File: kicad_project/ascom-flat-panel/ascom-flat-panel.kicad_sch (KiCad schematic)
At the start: 12 parts, among them J1 Servo, J3 JST-XH LED, Q1 FQP30N06L, Q2 FQP30N06L, U1 SeeeduinoXIAO

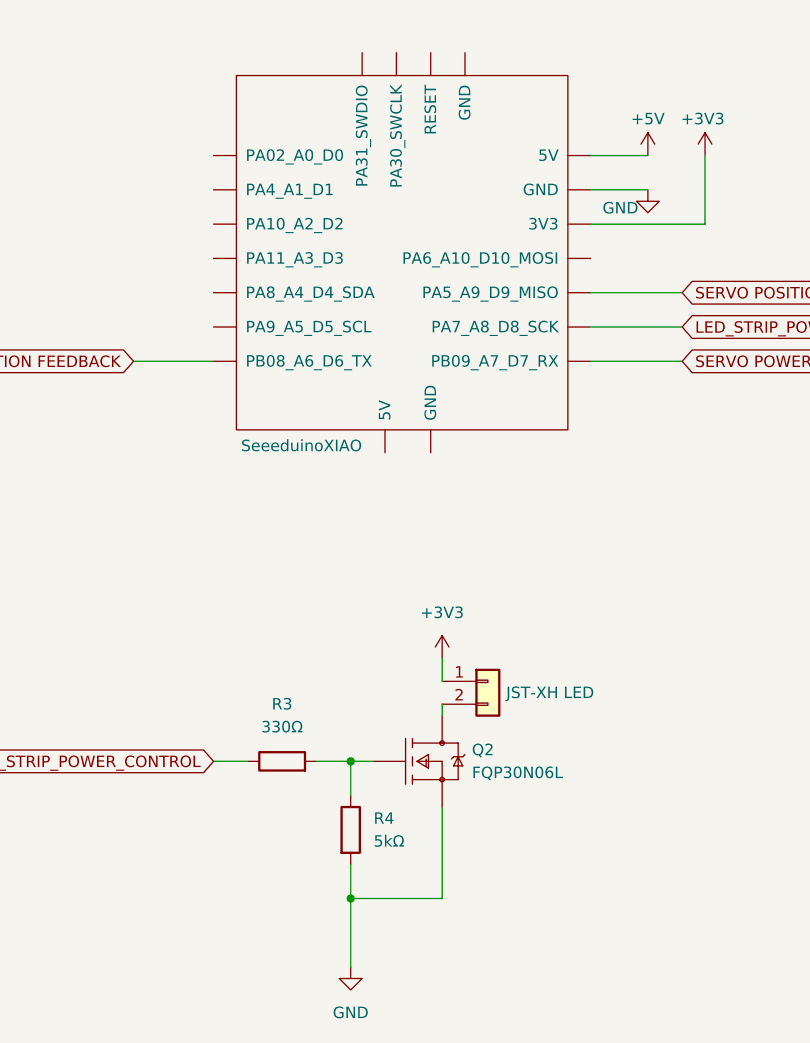
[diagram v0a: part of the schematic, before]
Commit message: ajout des bibliothèque de symboles et empreintes Seeeduino XIAO + mise à jour du schéma avec ces éléments + draft de pcb
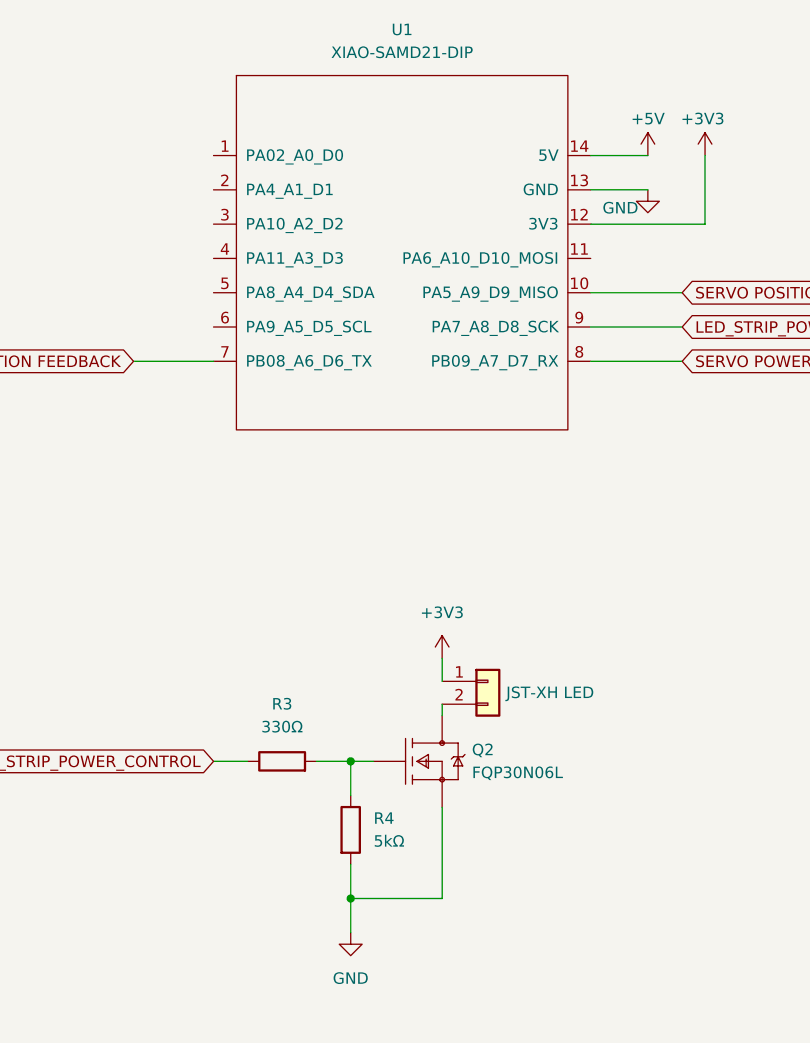
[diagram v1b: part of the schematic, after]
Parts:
- removed U1: SeeeduinoXIAO, Seeeduino XIAO:Seeeduino XIAO-MOUDLE14P-2.54-21X17.8MM, symbol Seeeduino XIAO:SeeeduinoXIAO
- added U1: XIAO-SAMD21-DIP, Seeeduino XIAO:XIAO-SAMD21-DIP, symbol Seeeduino:XIAO-SAMD21-DIP
- Q1, Q2: footprint MyFootprints:FQP30N06L -> Package_TO_SOT_THT:TO-220-3_Vertical
- R3, R4: footprint (none) -> Resistor_THT:R_Axial_DIN0207_L6.3mm_D2.5mm_P10.16mm_Horizontal
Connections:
- net +3V3: now also U1.12 (3V3)
- net +5V: now also U1.14 (5V)
- net GND: now also U1.13 (GND)
- net LED_STRIP_POWER_CONTROL: now also U1.9 (PA7_A8_D8_SCK)
- net SERVO POSITION CONTROL: now also U1.10 (PA5_A9_D9_MISO)
- net SERVO POSITION FEEDBACK: now also U1.7 (PB08_A6_D6_TX)
- net SERVO POWER CONTROL: now also U1.8 (PB09_A7_D7_RX)
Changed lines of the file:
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@@
 	(wire
 		(pts
-			(xy 78.74 127) (xy 78.74 134.62)
+			(xy 78.74 127) (xy 78.74 130.81)
 		)
 		(stroke
@@
 			)
 		)
-		(property "Footprint" ""
+		(property "Footprint" "Resistor_THT:R_Axial_DIN0207_L6.3mm_D2.5mm_P10.16mm_Horizontal"
 			(at 76.962 119.38 90)
 			(effects
@@
 	)
 	(symbol
-		(lib_id "Seeeduino XIAO:SeeeduinoXIAO")
-		(at 85.09 55.88 0)
-		(unit 1)
-		(exclude_from_sim no)
-		(in_bom yes)
-		(on_board yes)
-		(dnp no)
-		(property "Reference" "U1"
-			(at 89.8241 77.47 0)
-			(effects
-				(font
-					(size 1.27 1.27)
-				)
-				(justify left)
-				(hide yes)
-			)
-		)
-		(property "Value" "SeeeduinoXIAO"
-			(at 66.548 76.708 0)
-			(effects
-				(font
-					(size 1.27 1.27)
-				)
-				(justify left)
-			)
-		)
-		(property "Footprint" "Seeeduino XIAO:Seeeduino XIAO-MOUDLE14P-2.54-21X17.8MM"
-			(at 76.2 50.8 0)
-			(effects
-				(font
-					(size 1.27 1.27)
-				)
-				(hide yes)
-			)
-		)
-		(property "Datasheet" ""
-			(at 76.2 50.8 0)
-			(effects
-				(font
-					(size 1.27 1.27)
-				)
-				(hide yes)
-			)
-		)
-		(property "Description" ""
-			(at 85.09 55.88 0)
-			(effects
-				(font
-					(size 1.27 1.27)
-				)
-			)
-		)
-		(pin "12"
-		)
-		(pin "10"
-		)
-		(pin "16"
-		)
-		(pin "15"
-		)
-		(pin "2"
-		)
-		(pin "17"
-		)
-		(pin "3"
-		)
-		(pin "4"
-		)
-		(pin "5"
-		)
-		(pin "19"
-		)
-		(pin "18"
-		)
-		(pin "20"
-		)
-		(pin "8"
-		)
-		(pin "9"
-		)
-		(pin "6"
-		)
-		(pin "7"
-		)
-		(pin "14"
-		)
-		(pin "13"
-		)
-		(pin "11"
-		)
-		(pin "1"
-		)
-		(instances
-			(project "TelescopeCoverV2-Simple"
-				(path "/c93103f3-9ac9-4319-baa6-df31525a6c92"
-					(reference "U1")
-					(unit 1)
-				)
-			)
-		)
-	)
-	(symbol
 		(lib_id "DarkSkyGeek_KiCad_Symbol_Library:FQP30N06L")
 		(at 182.88 111.76 0)
@@
 			)
 		)
-		(property "Footprint" "MyFootprints:FQP30N06L"
+		(property "Footprint" "Package_TO_SOT_THT:TO-220-3_Vertical"
 			(at 182.88 99.06 0)
 			(effects
@@
 			)
 		)
-		(property "Footprint" ""
+		(property "Footprint" "Resistor_THT:R_Axial_DIN0207_L6.3mm_D2.5mm_P10.16mm_Horizontal"
 			(at 71.12 113.538 90)
 			(effects
@@
 				(path "/c93103f3-9ac9-4319-baa6-df31525a6c92"
 					(reference "#PWR02")
+					(unit 1)
+				)
+			)
+		)
+	)
+	(symbol
+		(lib_id "Seeeduino:XIAO-SAMD21-DIP")
+		(at 85.09 55.88 0)
+		(unit 1)
+		(exclude_from_sim no)
+		(in_bom yes)
+		(on_board yes)
+		(dnp no)
+		(fields_autoplaced yes)
+		(property "Reference" "U1"
+			(at 84.455 30.48 0)
+			(effects
+				(font
+					(size 1.27 1.27)
+				)
+			)
+		)
+		(property "Value" "XIAO-SAMD21-DIP"
+			(at 84.455 33.02 0)
+			(effects
+				(font
+					(size 1.27 1.27)
+				)
+			)
+		)
+		(property "Footprint" "Seeeduino XIAO:XIAO-SAMD21-DIP"
+			(at 76.2 50.8 0)
+			(effects
+				(font
+					(size 1.27 1.27)
+				)
+				(hide yes)
+			)
+		)
+		(property "Datasheet" ""
+			(at 76.2 50.8 0)
+			(effects
+				(font
+					(size 1.27 1.27)
+				)
+				(hide yes)
+			)
+		)
+		(property "Description" ""
+			(at 85.09 55.88 0)
+			(effects
+				(font
+					(size 1.27 1.27)
+				)
+				(hide yes)
+			)
+		)
+		(pin "3"
+		)
+		(pin "2"
+		)
+		(pin "5"
+		)
+		(pin "1"
+		)
+		(pin "14"
+		)
+		(pin "4"
+		)
+		(pin "6"
+		)
+		(pin "13"
+		)
+		(pin "12"
+		)
+		(pin "11"
+		)
+		(pin "10"
+		)
+		(pin "9"
+		)
+		(pin "8"
+		)
+		(pin "7"
+		)
+		(instances
+			(project ""
+				(path "/c93103f3-9ac9-4319-baa6-df31525a6c92"
+					(reference "U1")
 					(unit 1)
 				)
@@
 			)
 		)
-		(property "Footprint" "MyFootprints:FQP30N06L"
+		(property "Footprint" "Package_TO_SOT_THT:TO-220-3_Vertical"
 			(at 78.74 99.06 0)
 			(effects
@@
 		(lib_name "GND_1")
 		(lib_id "power:GND")
-		(at 78.74 134.62 0)
+		(at 78.74 130.81 0)
 		(unit 1)
 		(exclude_from_sim no)
@@
 		(fields_autoplaced yes)
 		(property "Reference" "#PWR09"
-			(at 78.74 140.97 0)
+			(at 78.74 137.16 0)
 			(effects
 				(font
@@
 		)
 		(property "Value" "GND"
-			(at 78.74 139.7 0)
+			(at 78.74 135.89 0)
 			(effects
 				(font
@@
 		)
 		(property "Footprint" ""
-			(at 78.74 134.62 0)
+			(at 78.74 130.81 0)
 			(effects
 				(font
@@
 		)
 		(property "Datasheet" ""
-			(at 78.74 134.62 0)
+			(at 78.74 130.81 0)
 			(effects
 				(font
@@
 		)
 		(property "Description" "Power symbol creates a global label with name \"GND\" , ground"
-			(at 78.74 134.62 0)
-			(effects
-				(font
+			(at 78.74 130.81 0)
+			(effects
+				(font

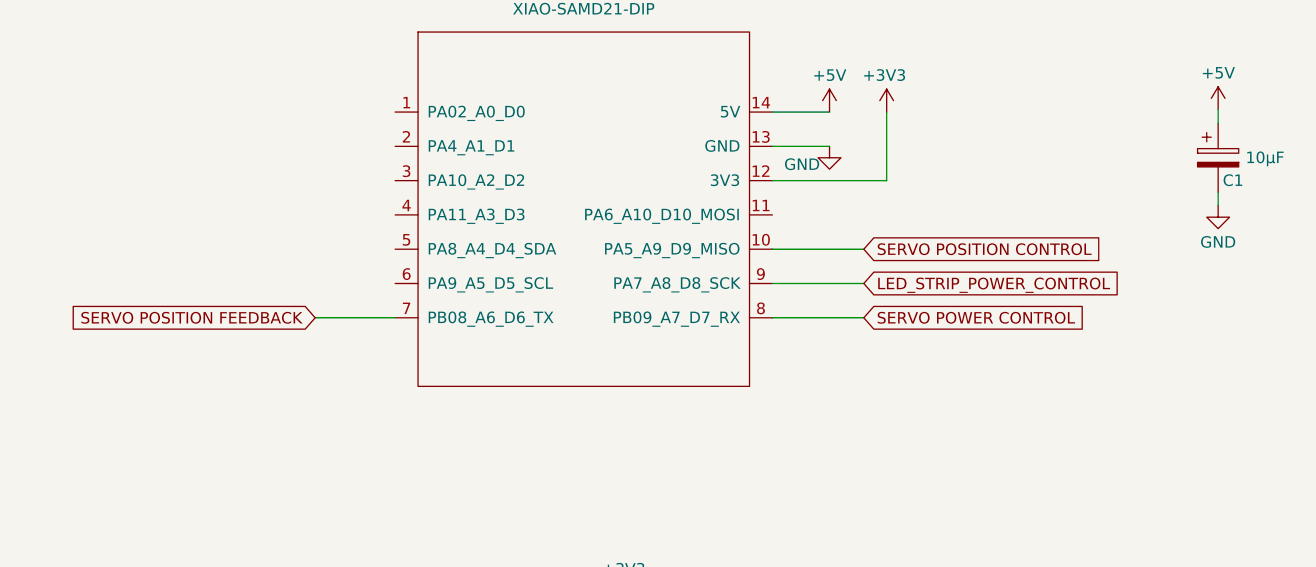
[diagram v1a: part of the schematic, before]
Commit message: Première mise en forme et routage du circuit - ajout modèle3D seeeduino
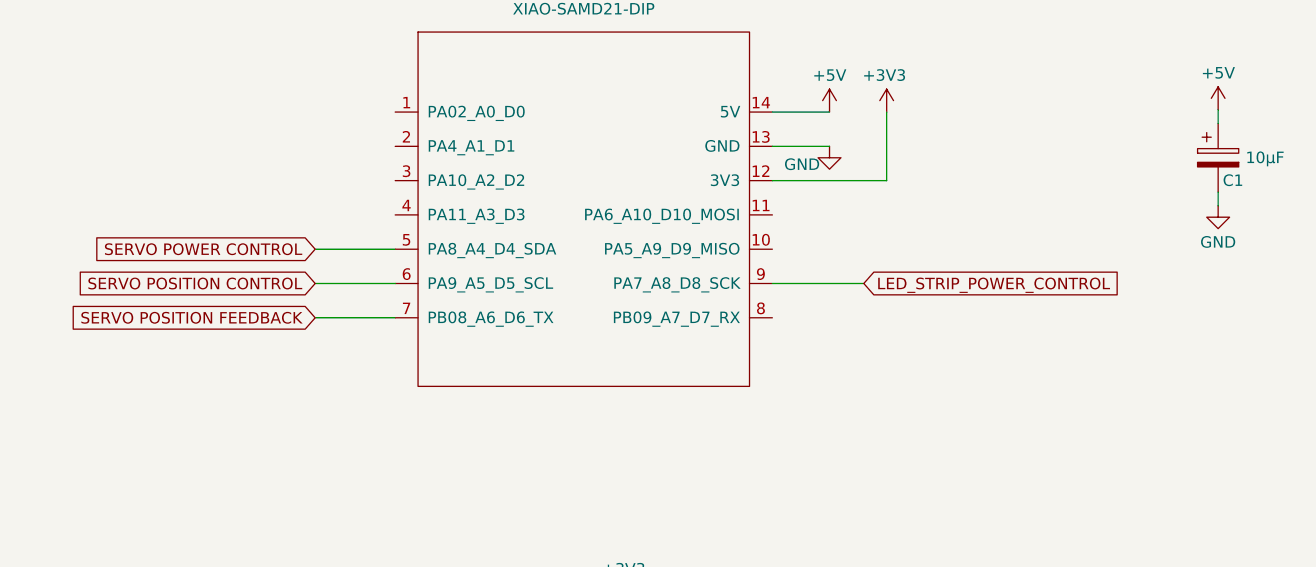
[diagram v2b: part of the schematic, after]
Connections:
- net SERVO POSITION CONTROL: now also U1.6 (PA9_A5_D5_SCL); no longer U1.10 (PA5_A9_D9_MISO)
- net SERVO POWER CONTROL: now also U1.5 (PA8_A4_D4_SDA); no longer U1.8 (PB09_A7_D7_RX)
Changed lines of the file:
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@@
-	(wire
-		(pts
-			(xy 105.41 67.31) (xy 115.57 67.31)
-		)
-		(stroke
-			(width 0)
-			(type default)
-		)
-	)
 	(wire
 		(pts
@@
 	(wire
 		(pts
+			(xy 54.61 59.69) (xy 63.5 59.69)
+		)
+		(stroke
+			(width 0)
+			(type default)
+		)
+	)
+	(wire
+		(pts
+			(xy 54.61 63.5) (xy 63.5 63.5)
+		)
+		(stroke
+			(width 0)
+			(type default)
+		)
+	)
+	(wire
+		(pts
 			(xy 182.88 111.76) (xy 185.42 111.76)
 		)
@@
 	(wire
 		(pts
-			(xy 105.41 59.69) (xy 115.57 59.69)
-		)
-		(stroke
-			(width 0)
-			(type default)
-		)
-	)
-	(wire
-		(pts
 			(xy 193.04 46.482) (xy 198.12 46.482)
 		)
@@
 	(global_label "SERVO POWER CONTROL"
 		(shape input)
-		(at 115.57 67.31 0)
-		(fields_autoplaced yes)
-		(effects
-			(font
-				(size 1.27 1.27)
-			)
-			(justify left)
-		)
-		(property "Intersheetrefs" "${INTERSHEET_REFS}"
-			(at 141.5361 67.31 0)
-			(effects
-				(font
-					(size 1.27 1.27)
-				)
-				(justify left)
+		(at 54.61 59.69 180)
+		(fields_autoplaced yes)
+		(effects
+			(font
+				(size 1.27 1.27)
+			)
+			(justify right)
+		)
+		(property "Intersheetrefs" "${INTERSHEET_REFS}"
+			(at 28.6439 59.69 0)
+			(effects
+				(font
+					(size 1.27 1.27)
+				)
+				(justify right)
 				(hide yes)
 			)
@@
 	(global_label "SERVO POSITION CONTROL"
 		(shape input)
-		(at 115.57 59.69 0)
-		(fields_autoplaced yes)
-		(effects
-			(font
-				(size 1.27 1.27)
-			)
-			(justify left)
-		)
-		(property "Intersheetrefs" "${INTERSHEET_REFS}"
-			(at 143.7134 59.69 0)
-			(effects
-				(font
-					(size 1.27 1.27)
-				)
-				(justify left)
-				(hide yes)
-			)
+		(at 54.61 63.5 180)
+		(fields_autoplaced yes)
+		(effects
+			(font
+				(size 1.27 1.27)
+			)
+			(justify right)
+		)
+		(property "Intersheetrefs" "${INTERSHEET_REFS}"
+			(at 26.4666 63.5 0)
+			(effects
+				(font
+					(size 1.27 1.27)
+				)
+				(justify right)
+				(hide yes)
+			)

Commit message: Remplissage cartouche du schéma
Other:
- company: (none) -> Le Télescope - Ivry. Heavily inspired by the the work of Dark Sky Geek (https://github.com/jlecomte/)
- title: (none) -> FFFP (Florian & Florian Flat Panel)
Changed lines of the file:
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@@
 	(generator_version "9.0")
 	(paper "A4")
+	(title_block
+		(title "FFFP (Florian & Florian Flat Panel)")
+		(date "2025-03-31")
+		(rev "1")
+		(company "Le Télescope - Ivry. Heavily inspired by the the work of Dark Sky Geek (https://github.com/jlecomte/)")
+		(comment 1 "rev 1 - Bon pour tests sur planche de prototypage")
+	)
 	(junction
 		(at 182.88 111.76)

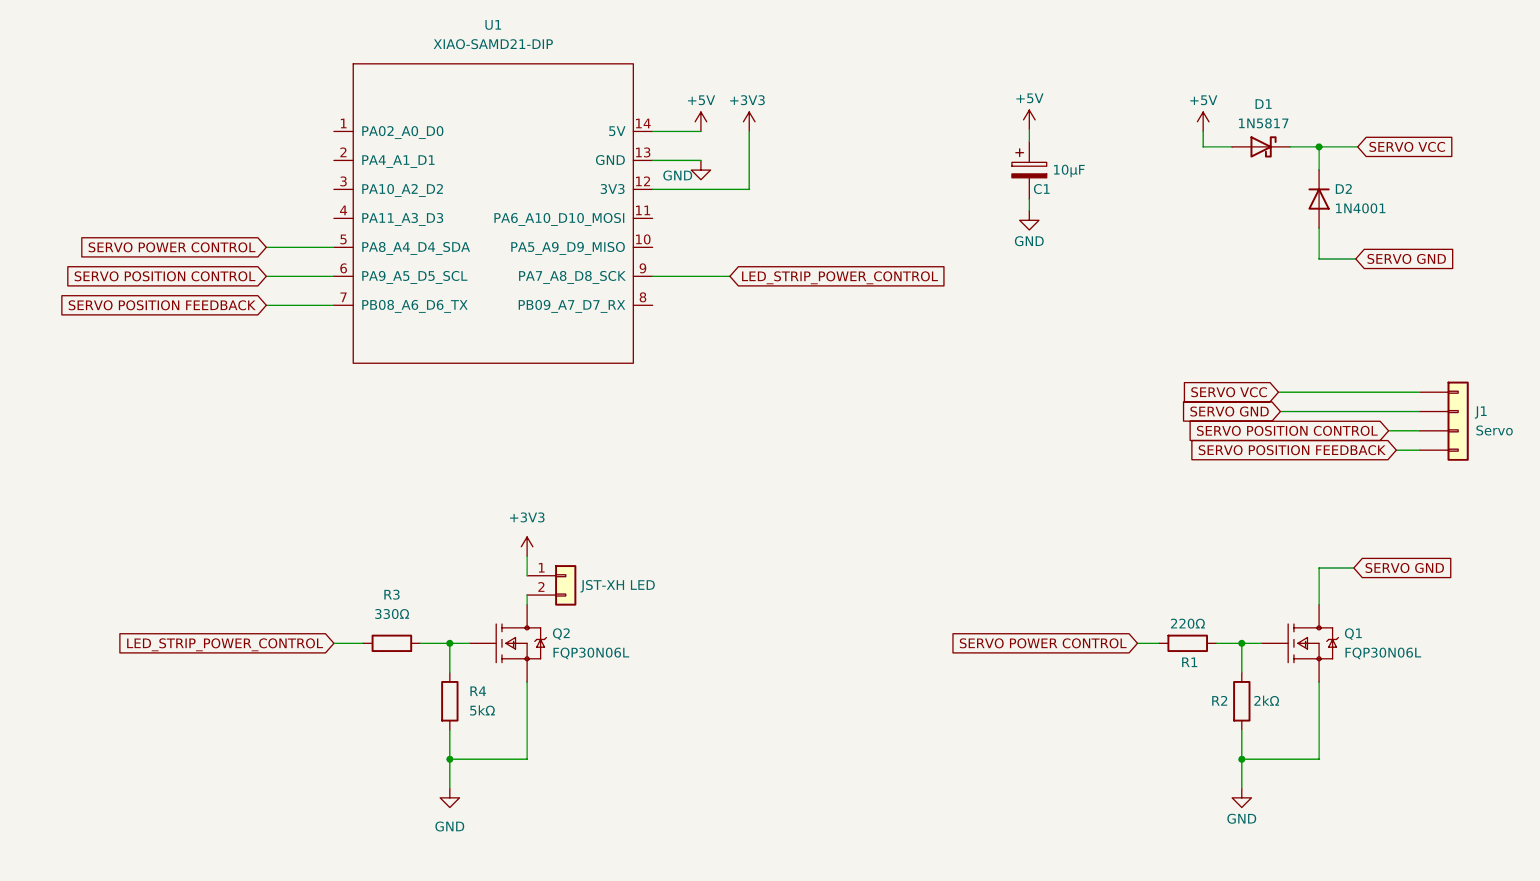
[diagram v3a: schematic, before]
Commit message: Mise à jour des références des diodes et MOSFET suivant composants achetés. TODO : vérifier pas et diamètre de C1 - ajuster empreinte le cas échéant
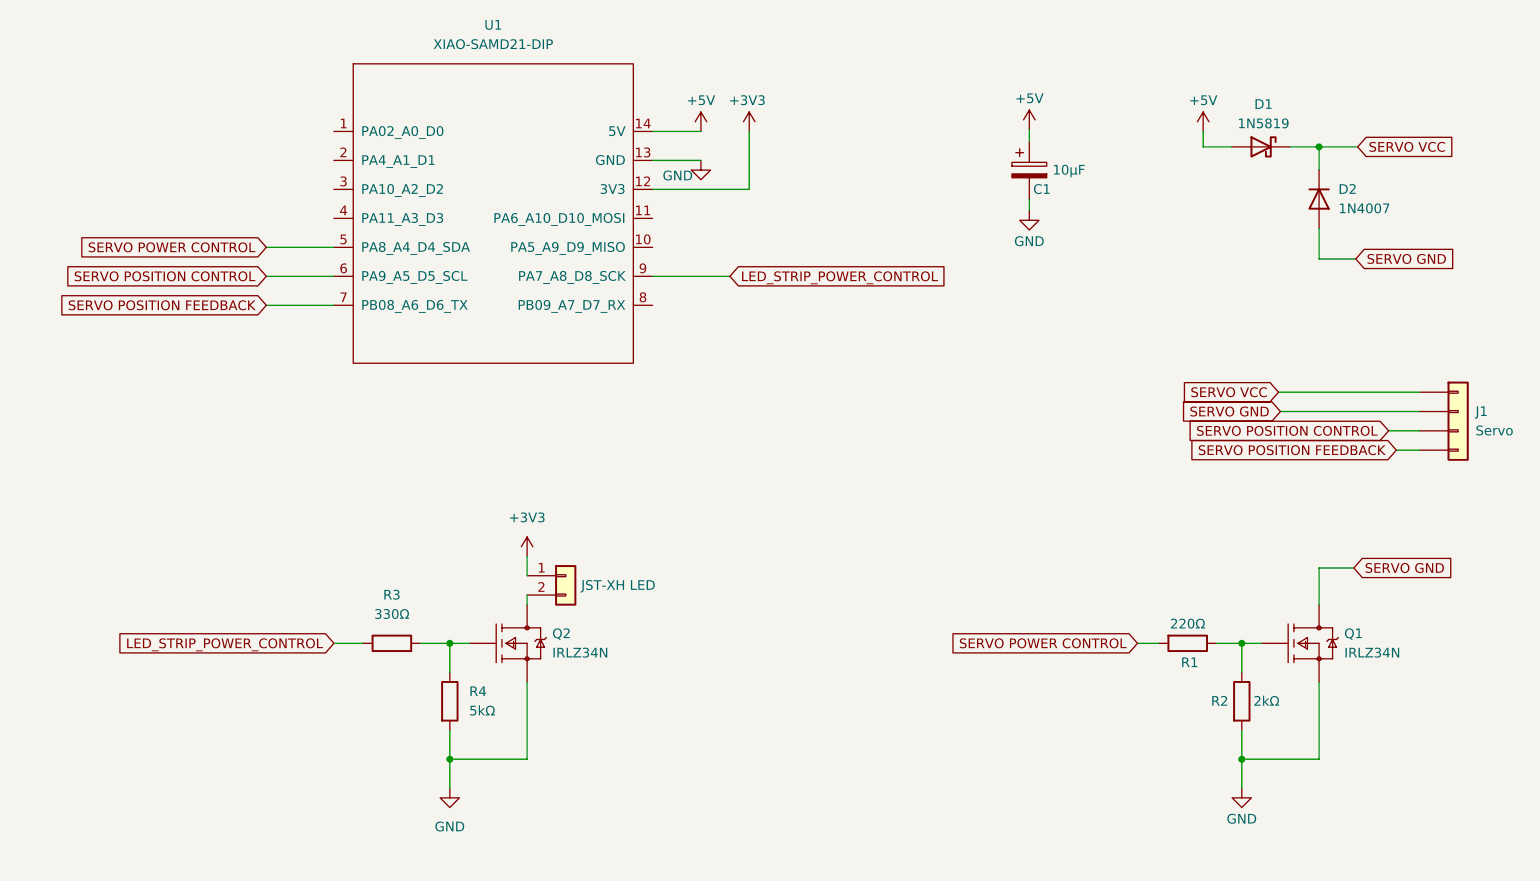
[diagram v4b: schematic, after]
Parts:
- D1: value 1N5817 -> 1N5819
- D2: value 1N4001 -> 1N4007
- Q1, Q2: value FQP30N06L -> IRLZ34N
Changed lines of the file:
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@@
 			)
 		)
-		(property "Value" "FQP30N06L"
+		(property "Value" "IRLZ34N"
 			(at 196.342 113.03 0)
 			(effects
@@
 			)
 		)
-		(property "Value" "1N5817"
+		(property "Value" "1N5819"
 			(at 185.7375 43.434 0)
 			(effects
@@
 		(fields_autoplaced yes)
 		(property "Reference" "D2"
-			(at 195.072 52.07 90)
-			(effects
-				(font
-					(size 1.27 1.27)
-				)
-				(justify left)
-			)
-		)
-		(property "Value" "1N4001"
-			(at 195.072 54.61 90)
+			(at 195.58 52.0699 90)
+			(effects
+				(font
+					(size 1.27 1.27)
+				)
+				(justify left)
+			)
+		)
+		(property "Value" "1N4007"
+			(at 195.58 54.6099 90)
 			(effects
 				(font
@@
 			)
 		)
-		(property "Value" "FQP30N06L"
+		(property "Value" "IRLZ34N"
 			(at 92.202 113.03 0)
 			(effects

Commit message: [kicad] - changements de variables d'environnement pour garantir la portabilité du projet. La bibliothèque d'empreintes et le modèle 3D sont en outre déplacés dans le répertoire du projet. A TESTER !
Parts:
- U1: footprint Seeeduino XIAO:XIAO-SAMD21-DIP -> SEEED_STUDIO:XIAO-SAMD21-DIP
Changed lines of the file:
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@@
 			)
 		)
-		(property "Footprint" "Seeeduino XIAO:XIAO-SAMD21-DIP"
+		(property "Footprint" "SEEED_STUDIO:XIAO-SAMD21-DIP"
 			(at 76.2 50.8 0)
 			(effects
